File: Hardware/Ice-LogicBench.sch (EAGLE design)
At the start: 114 parts, among them IC1 S27KL0641DABHV020, IC2 S26KL128SDABHI020, IC3 USBLC6-2SC6, IC4 ICE40HX4K-BG121, IC5 FUSB302MPX, IC6 USBLC6-2SC6, J2 QWIIC_RIGHT_ANGLE, Y3 12MZ

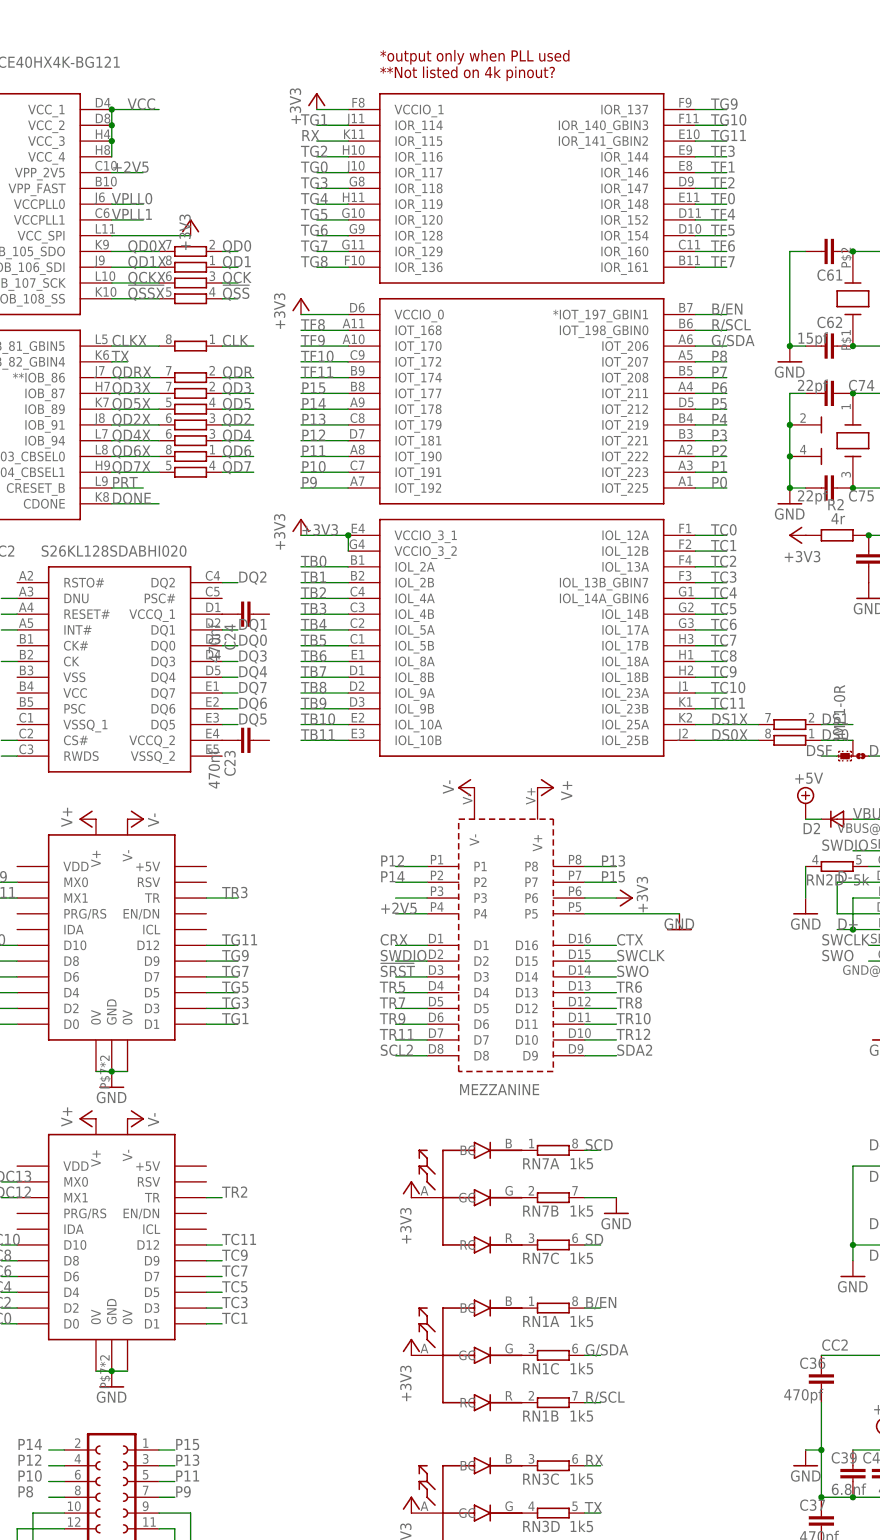
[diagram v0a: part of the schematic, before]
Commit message: REarranged TG/F pinouts for pait matches updated schematic and previews
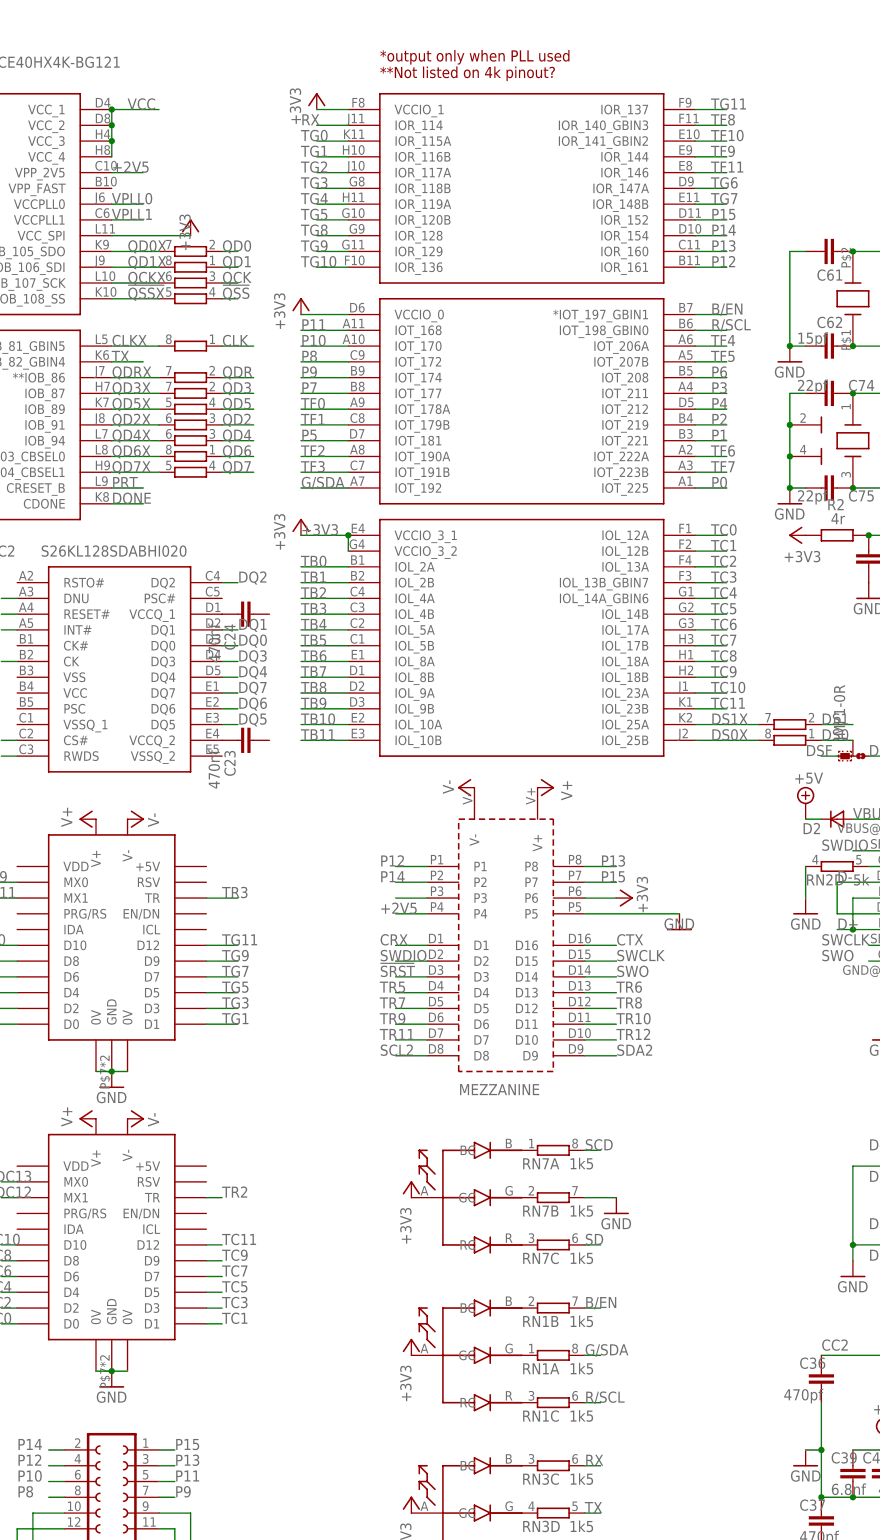
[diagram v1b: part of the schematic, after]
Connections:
- net B/EN: now also RN1B.2; no longer RN1A.2
- net G/SDA: now also IC4.IOT_192, RN1A.2; no longer IC4.IOT_206, RN1C.2
- net N$1: now also RN1A.1; no longer RN1C.1
- net N$3: now also RN1C.1; no longer RN1B.1
- net N$5: now also RN1B.1; no longer RN1A.1
- net P1: now also IC4.IOT_221; no longer IC4.IOT_223
- net P10: now also IC4.IOT_170; no longer IC4.IOT_191
- net P11: now also IC4.IOT_168; no longer IC4.IOT_190
- net P12: now also IC4.IOR_161; no longer IC4.IOT_181
- net P13: now also IC4.IOR_160; no longer IC4.IOT_179
- net P14: now also IC4.IOR_154; no longer IC4.IOT_178
- net P15: now also IC4.IOR_152; no longer IC4.IOT_177
- net P2: now also IC4.IOT_219; no longer IC4.IOT_222
- net P3: now also IC4.IOT_211; no longer IC4.IOT_221
- net P4: now also IC4.IOT_212; no longer IC4.IOT_219
- net P5: now also IC4.IOT_181; no longer IC4.IOT_212
- net P6: now also IC4.IOT_208; no longer IC4.IOT_211
- net P7: now also IC4.IOT_177; no longer IC4.IOT_208
- net P8: now also IC4.IOT_172; no longer IC4.IOT_207
- net P9: now also IC4.IOT_174; no longer IC4.IOT_192
- net R/SCL: now also RN1C.2; no longer RN1B.2
- net RX: now also IC4.IOR_114; no longer IC4.IOR_115
- net TF0: now also IC4.IOT_178A; no longer IC4.IOR_148
- net TF1: now also IC4.IOT_179B; no longer IC4.IOR_146
- net TF10: now also IC4.IOR_141_GBIN2; no longer IC4.IOT_172
- net TF11: now also IC4.IOR_146; no longer IC4.IOT_174
- net TF2: now also IC4.IOT_190A; no longer IC4.IOR_147
- net TF3: now also IC4.IOT_191B; no longer IC4.IOR_144
- net TF4: now also IC4.IOT_206A; no longer IC4.IOR_152
- net TF5: now also IC4.IOT_207B; no longer IC4.IOR_154
- net TF6: now also IC4.IOT_222A; no longer IC4.IOR_160
- net TF7: now also IC4.IOT_223B; no longer IC4.IOR_161
- net TF8: now also IC4.IOR_140_GBIN3; no longer IC4.IOT_168
- net TF9: now also IC4.IOR_144; no longer IC4.IOT_170
- net TG0: now also IC4.IOR_115A; no longer IC4.IOR_117
- net TG1: now also IC4.IOR_116B; no longer IC4.IOR_114
- net TG10: now also IC4.IOR_136; no longer IC4.IOR_140_GBIN3
- net TG11: now also IC4.IOR_137; no longer IC4.IOR_141_GBIN2
- net TG2: now also IC4.IOR_117A; no longer IC4.IOR_116
- net TG3: now also IC4.IOR_118B; no longer IC4.IOR_118
- net TG4: now also IC4.IOR_119A; no longer IC4.IOR_119
- net TG5: now also IC4.IOR_120B; no longer IC4.IOR_120
- net TG6: now also IC4.IOR_147A; no longer IC4.IOR_128
- net TG7: now also IC4.IOR_148B; no longer IC4.IOR_129
- net TG8: now also IC4.IOR_128; no longer IC4.IOR_136
- net TG9: now also IC4.IOR_129; no longer IC4.IOR_137
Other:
- moved on the sheet: RN1A, RN1B, RN1C

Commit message: Temporarily added book by disabling the git ignore until I cal work out the continuous Integration required
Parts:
- removed C30, C43, C74, C75: 22pf, rcl:C-EUC0402
- removed C35, C40, C41, C67, C68, C69, C70, C72: 470nf, rcl:C-EUC0402
- removed C36, C37: 470pf, rcl:C-EUC0402
- removed C38: (no value), rcl:CPOL-EUUD-6,3X8,8
- removed C39: 6.8nf, rcl:C-EUC0402
- removed C42: 22uf, rcl:C-EUC0603
- removed C61, C62: 15pf, rcl:C-EUC0402
- removed C71: 4u7, rcl:C-EUC0402
- removed CAM1, LCD: FH12-24S-0.5SH, con-hirose:FH12-24S-0.5SH
- removed D1: (no value), diode:DIODE-DO214AC
- removed D2: (no value), zetex:DSOD323
- removed D3: (no value), diode:DIODE-SOD323-R
- removed DEBUG: (no value), pinhead:PINHD-2X3/90
- removed H2: HOLE2.5MM-LARGE, amino:HOLE2.5MM-LARGE
- removed J2: QWIIC_RIGHT_ANGLE, SparkFun-Connectors:QWIIC_CONNECTORJS-1MM
- removed JMP1, JMP2: 0R-JUMPC, jump-0r-smd:0R-JUMPC
- removed MEZZANINE: HYPER-TILE, amino:HYPER-TILE
- removed R10: 150k, resistor:R-EU_R0402
- removed RN10, RN11, RN12: 22r, resistor-dil:4R-NEXB38V
- removed SV1, SV2: (no value), con-lsta:FE06-2W
- removed U$11: AT25SDF041A, amino:AT25SDF041A
- removed U$12, U$17: RGB_LED0805, amino:RGB_LED0805
- removed U$20, U$6: (no value), amino:AP3429/A
- removed U$8: USB-C-16, amino:USB-C-16
- removed U$9: NCP114, amino:NCP114
- added B1: PUSH_BUTTON, amino:PUSH_BUTTON
- added BT100: (no value), SparkFun-Batteries:BATTERY-20MM_SMD
- added C100, C102, C103, C104, C106, C107, C108, C109, C110, C111, C112: 470nf, rcl:C-EUC0402
- added C101, C105, C113: 4u7, rcl:C-EUC0402
- added CN1, CN2: USB-C-16, amino:USB-C-16
- added CN3: 2X5-HEADER, amino:2X5-HEADER
- added IC10: FUSB302MPX, SamacSys_Parts:FUSB302MPX
- added IC7, IC8: USBLC6-2SC6, SamacSys_Parts:USBLC6-2SC6
- added J1: QWIIC_RIGHT_ANGLE, SparkFun-Connectors:QWIIC_CONNECTORJS-1MM
- added L1: RGB_LED, amino:RGB_LED
- added L2: (no value), led:LEDCHIPLED_1206
- added R7: 100r, resistor:R-EU_R0402
- added R8: 1k5, resistor:R-EU_R0402
- added RN100, RN101, RN102: 10k, resistor-dil:4R-NEXB38V
- added TILE2: UTILE_LPCARRIER_SMD_MALE_1.27, amino:UTILE_LPCARRIER_SMD_MALE_1.27
- added TILE6: HYPER-TILECARRIER, amino:HYPER-TILECARRIER
- C1, C12, C2, C20, C3, C6: value 470nf -> 22uf; device rcl:C-EUC0402 -> rcl:C-EUC0603
- C11, C27, C5: value 470nf -> 22pf
- C13, C15, C31, C34: value 6.8nf -> 470nf
- C19: value 4u7 -> 22uf; device rcl:C-EUC0402 -> rcl:C-EUC0603
- C21: value 10uf -> 470nf
- C25: value 470nf -> 4u7
- C26: value 22uf -> 15pf; device rcl:C-EUC0603 -> rcl:C-EUC0402
- C28: value 470nf -> 15pf
- C29: value 22uf -> 22pf; device rcl:C-EUC0603 -> rcl:C-EUC0402
- C32, C33: value 6.8nf -> 470pf
- IC1: value S27KL0641DABHV020 -> (none); device SamacSys_Parts:S27KL0641DABHV020 -> amino:AP3429/A
- IC2: value S26KL128SDABHI020 -> NCP114; device SamacSys_Parts:S26KL128SDABHI020 -> amino:NCP114
- IC3: value USBLC6-2SC6 -> ICE40HX4K-BG121; device SamacSys_Parts:USBLC6-2SC6 -> SamacSys_Parts:ICE40HX4K-BG121
- IC4: value ICE40HX4K-BG121 -> AT25SDF041A; device SamacSys_Parts:ICE40HX4K-BG121 -> amino:AT25SDF041A
- IC5: value FUSB302MPX -> (none); device SamacSys_Parts:FUSB302MPX -> amino:AP3429/A
- IC6: value USBLC6-2SC6 -> S27KL0641DABHV020; device SamacSys_Parts:USBLC6-2SC6 -> SamacSys_Parts:S27KL0641DABHV020
- R1: value 27k -> 120k
- R2: value 4r -> 120k
- R3, R4: value 100R -> 100r
- R6: value 100R -> 27k
- R9: value 120k -> 1k
- RN1, RN3: value 1k5 -> 22r
- RN2, RN5: value 5k -> 22r; device resistor-dil:4R-N0603-ARV -> resistor-dil:4R-NEXB38V
- RN4: value 5.1k -> 22r
- RN6, RN9: value 22r -> 5k1
- RN7: value 1k5 -> 5k1
- RN8: value 22r -> 1k5
- U$1: value USB-C-16 -> SS54; device amino:USB-C-16 -> amino:SS54
- U$2: value RGB_LED0805 -> SS54; device amino:RGB_LED0805 -> amino:SS54
- renumbered QD6 to IC9, R14 to R5, U$10 to SD100, U$13 to TILE5, U$23 to I1, U$3 to TILE1, U$30 to TILE3, U$31 to TILE4, U$4 to Y2, U$7 to I2, Y3 to Y1
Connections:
- removed net !CS: IC9.PE15
- removed net !INT: IC5.INT_N
- removed net ADC2/MISO1: IC9.PC2
- removed net ADC3/MOSI1: IC9.PC3
- removed net ADC8/DHS: IC9.PA4
- removed net B/EN: CAM1-17.1, IC4.*IOT_197_GBIN1, RN1B.2
- removed net CC1: C37.1, IC5.CC1_1, IC5.CC1_2, IC6.I/O1_2, U$8.CC1
- removed net CC2: C36.2, IC5.CC2_1, IC5.CC2_2, IC6.I/O2_2, U$8.CC2
- removed net CRX: IC9.PB12, MEZZANINE.D1
- removed net CTX: IC9.PB13, MEZZANINE.D16
- removed net DC2: IC9.PE0
- removed net DC3: IC9.PE1
- removed net DC5: IC9.PD3
- removed net DN: U$8.DN1, U$8.DN2
- removed net DS1: IC1.CS#, RN8B.1
- removed net DS1X: IC4.IOL_25A, RN8B.2
- removed net DSF: IC2.CS#, JMP1-0R.1
- removed net DSR: IC2.DNU, JMP1-0R.3
- removed net DVS: IC9.PB7
- removed net G/SDA: CAM1-22.1, IC4.IOT_192, RN1A.2
- removed net INT: IC2.INT#
- removed net N$15: C23.1, IC2.VCCQ_2
- removed net N$16: C24.1, IC2.VCCQ_1
- removed net N$17: C25.1, IC1.VCCQ_1
- removed net N$20: RN7A.1, U$12.BC
- removed net N$21: RN7B.1, U$12.GC
- removed net N$22: RN7C.1, U$12.RC
- removed net N$23: LCD-1.1, R4.1
- removed net N$24: RN7D.2, U$8.SHLD
- removed net N$25: C41.2, IC9.VDD_2
- removed net N$26: CAM1-23.1, JMP2-0R.2
- removed net N$27: IC3.I/O1_2
- removed net N$28: IC3.I/O2_2
- removed net N$3: RN1C.1, U$17.RC
- removed net N$5: RN1B.1, U$17.BC
- removed net N$7: MEZZANINE.P3
- removed net N$8: RN3A.2, U$1.SHLD
- removed net N$85: C69.2, IC9.VDD_4
- removed net N$86: C67.2, IC9.VDD_3
- removed net N$89: C68.2, IC9.VDD_5
- removed net N$9: RN2D.2, U$1.CC1
- removed net N$90: C71.1, IC9.VBAT
- removed net N$92: C19.1, IC9.VREF+
- removed net QD4: IC9.PD11, RN10C.1
- removed net QD4X: IC4.IOB_94, RN10C.2
- removed net QD5: IC9.PD12, RN10D.1
- removed net QD5X: IC4.IOB_89, RN10D.2
- removed net QD6: IC9.PE2, RN11A.1
- removed net QD6X: IC4.IOB_103_CBSEL0, RN11A.2
- removed net QD7: IC9.PD13, RN11D.1
- removed net QD7X: IC4.IOB_104_CBSEL1, RN11D.2
- removed net QDRX: IC4.**IOB_86, RN10B.2
- removed net R/SCL: CAM1-20.1, IC4.IOT_198_GBIN0, RN1C.2
- removed net TR10: IC9.PD7, MEZZANINE.D11
- removed net TR11: IC9.PB4, MEZZANINE.D7
- removed net TR12: IC9.PB5, MEZZANINE.D10
- removed net TR7: IC9.PD4, MEZZANINE.D5
- removed net TR8: IC9.PD5, MEZZANINE.D12
- removed net TR9: IC9.PD6, MEZZANINE.D6
- removed net V+: C38.+, D1.C, H2.P, H4.P, MEZZANINE.V+, TILE1.V+, TILE3.V+, TILE4.V+, TILE5.V+
- removed net V-: C38.-, H1.P, H3.P, MEZZANINE.V-, TILE1.V-, TILE3.V-, TILE4.V-, TILE5.V-
- removed net VBUS: D2.A, IC3.VBUS, IC6.VBUS, U$1.VBUS
- removed net ~1V8: C31.2, CAM1-15.1, D3.C
- new net !HRST: IC6.RESET#, IC9.PD0
- new net !TRSTA: IC9.PE0, TILE1.PRG/RS, TILE2.PRG/RS, TILE4.PRG/RS
- new net !TRSTB: IC9.PE7, TILE3.PRG/RS, TILE5.PRG/RS
- new net ADC2: IC9.PC2, TILE4.RSV
- new net ADC3: IC9.PC3, TILE1.MX0
- new net B/!WS: IC3.*IOT_197_GBIN1, RN8C.2, TILE6.F23
- new net CC1A: CN1.CC1, RN9B.2, TILE6.E10
- new net CC1B: C33.1, CN2.CC1, IC10.CC1_1, IC10.CC1_2
- new net CC2A: CN1.CC2, RN9A.2, TILE6.E9
- new net CC2B: C32.2, CN2.CC2, IC10.CC2_1, IC10.CC2_2
- new net ENA: IC9.PE1, TILE1.EN/DN, TILE2.EN/DN, TILE4.EN/DN
- new net ENB: IC9.PE8, TILE3.EN/DN, TILE5.EN/DN
- new net G/MT1: IC3.IOT_181, TILE6.F2
- new net GP1: IC9.PD1, TILE6.E23
- new net GP2: IC9.PD3, TILE6.E2
- new net GP3: IC9.PD4, TILE6.E22
- new net GP4: IC9.PD5, TILE6.E3
- new net GP5: IC9.PD6, TILE6.E21
- new net GP6: IC9.PB4, TILE6.E4
- new net GP7: IC9.PB5, TILE6.E19
- new net GP8: IC9.PB7, TILE6.E6
- new net HLD: IC4.HOLD, IC9.PE15
- new net INTU: IC10.INT_N, IC9.PA4
- new net MODE: IC9.PE9, RN8B.2
- new net MT0: IC3.IOR_114, TILE6.F1
- new net R/!DS: IC3.IOT_198_GBIN0, TILE6.F24
- new net RXX: IC3.IOL_25B, RN1A.2
- new net SHA: CN1.SHLD, R8.1
- new net SHB: CN2.SHLD, RN8D.1
- new net TXX: IC3.IOL_25A, RN1B.2
- new net VBAT: BT100.+, C23.1, IC9.VBAT
- new net VBUSA: CN1.VBUS, IC8.VBUS, TILE6.E15, U$2.ANODE
- new net VBUSB: CN2.VBUS, IC10.VBUS, U$1.ANODE
- new net WP: IC4.WP, IC9.PE10
- net !QSS: now also RN4C.1; no longer RN12D.1
- net !QSSX: now also IC3.IOB_104_CBSEL1, RN5D.2; no longer IC4.IOB_108_SS, RN12D.2
- net !SRST: now also C24.2, CN3.6, RN7D.2, TILE6.E17; no longer DEBUG.4, MEZZANINE.D3
- net !SS: now also IC3.IOB_108_SS, IC4.CS, RN102D.1; no longer RN4B.1, U$11.CS
- net +2V5: now also C112.1, C7.2, IC2.VOUT, IC3.VPP_2V5; no longer C27.2, C33.2, C5.1, CAM1-21.1, D3.A, IC4.VPP_2V5, MEZZANINE.P4, U$9.VOUT
- net +3V3: now also B1.P$1, C100.1, C101.2, C102.1, C103.1, C106.1, C108.1, C11.2, C16.2, C17.2, C2.1, C22.2, C3.2, C31.2, C6.2, C8.2, CN3.1, IC10.VDD_1, IC10.VDD_2, IC2.EN, IC2.VIN, IC3.VCCIO_0, IC3.VCCIO_1, IC3.VCCIO_2, IC3.VCCIO_3_1, IC3.VCCIO_3_2, IC3.VCC_SPI, IC4.VCC, IC6.VCCQ_1, IC6.VCCQ_2, IC9.VDD_2, IC9.VDD_3, IC9.VDD_4, IC9.VDD_5, J1.2, L1.ANODE, R7.2, R9.1, RN100A.2, RN100B.2, RN100C.2, RN101A.2, RN101B.2, RN101C.2, RN101D.2, RN102A.2, RN102B.2, RN102C.2, RN102D.2, RN6A.1, RN6B.1, RN7A.1, RN7B.1, RN7C.1, RN7D.1, TILE1.VDD, TILE2.VDD, TILE3.VDD, TILE4.VDD, TILE5.VDD, TILE6.F22; no longer C11.1, C14.2, C18.1, C20.1, C28.2, C29.1, C30.2, C32.2, C34.2, C35.2, C8.1, CAM1-14.1, DEBUG.6, IC4.VCCIO_0, IC4.VCCIO_1, IC4.VCCIO_2, IC4.VCCIO_3_1, IC4.VCCIO_3_2, IC4.VCC_SPI, IC5.VDD_1, IC5.VDD_2, J2.2, JMP2-0R.1, LCD-4.1, LCD-5.1, LCD-6.1, MEZZANINE.P6, R2.2, R4.2, RN1D.2, RN2A.2, RN2B.2, RN4A.2, RN4B.2, RN4C.2, RN4D.2, RN5A.2, RN5B.2, RN5C.2, RN5D.2, SV1.11, SV1.12, SV2.11, SV2.12, U$11.HOLD, U$11.VCC, U$11.WP, U$12.ANODE, U$17.ANODE, U$2.ANODE, U$9.EN, U$9.VIN
- net +5V: now also C1.2, C14.2, C20.1, C34.2, H1.P, IC1.VIN, IC10.VCONN_1, IC10.VCONN_2, IC5.EN, IC5.VIN, IC7.VBUS, TILE1.+5V, TILE2.+5V, TILE3.+5V, TILE4.+5V, TILE5.+5V, TILE6.E11, TILE6.E12, U$2.CATHODE; no longer C26.2, C39.2, C40.2, C42.2, D2.C, IC5.VCONN_1, IC5.VCONN_2, U$20.VIN, U$6.EN, U$6.VIN
- net ADC0: now also TILE4.MX0
- net ADC1: now also TILE4.MX1
- net ADC11: now also TILE3.MX0; no longer TILE5.MX1
- net ADC12: now also TILE3.MX1; no longer TILE4.MX1
- net ADC13: now also TILE3.RSV; no longer TILE4.MX0
- net ADC14: now also TILE2.MX0; no longer TILE1.MX1
- net ADC15: now also TILE2.MX1; no longer TILE1.MX0
- net ADC4: now also TILE1.MX1
- net ADC5: now also TILE1.RSV
- net ADC6: now also TILE5.MX0; no longer TILE3.MX0
- net ADC7: now also TILE5.MX1; no longer TILE3.MX1
- net ADC9: now also TILE5.RSV; no longer TILE5.MX0
- net BOOT: now also B1.P$2, IC9.PD7, RN100D.2, TILE6.E16; no longer RN2C.2
- net CLK: now also RN3D.1; no longer RN10A.1
- net CLKX: now also IC3.*IOB_81_GBIN5, RN3D.2; no longer IC4.*IOB_81_GBIN5, RN10A.2
- net D+: now also CN1.DP1, CN1.DP2, IC8.I/O1_2; no longer IC3.I/O2_1, U$1.DP1, U$1.DP2
- net D-: now also CN1.DN1, CN1.DN2, IC8.I/O2_2; no longer IC3.I/O1_1, U$1.DN1, U$1.DN2
- net DM: now also CN2.DN1, CN2.DN2, IC7.I/O1_1; no longer IC6.I/O1_1
- net DONE: now also IC3.CDONE, IC9.PD14, RN8A.2; no longer IC4.CDONE, IC9.PD15, RN3B.2
- net DP: now also CN2.DP1, CN2.DP2, IC7.I/O2_1; no longer IC6.I/O2_1, U$8.DP1, U$8.DP2
- net DQ0: now also IC6.DQ0, RN2B.1; no longer IC1.DQ0, IC2.DQ0, RN6B.1
- net DQ0X: now also IC3.IOB_63, RN2B.2; no longer IC4.IOB_63, RN6B.2
- net DQ1: now also IC6.DQ1, RN3A.1; no longer IC1.DQ1, IC2.DQ1, RN9B.1
- net DQ1X: now also IC3.IOB_73, RN3A.2; no longer IC4.IOB_73, RN9B.2
- net DQ2: now also IC6.DQ2, RN1C.1; no longer IC1.DQ2, IC2.DQ2, RN8C.1
- net DQ2X: now also IC3.IOB_56, RN1C.2; no longer IC4.IOB_56, RN8C.2
- net DQ3: now also IC6.DQ3, RN4A.1; no longer IC1.DQ3, IC2.DQ3, RN9A.1
- net DQ3X: now also IC3.IOB_79, RN4A.2; no longer IC4.IOB_79, RN9A.2
- net DQ4: now also IC6.DQ4, RN1D.1; no longer IC1.DQ4, IC2.DQ4, RN8D.1
- net DQ4X: now also IC3.IOB_57, RN1D.2; no longer IC4.IOB_57, RN8D.2
- net DQ5: now also IC6.DQ5, RN2C.1; no longer IC1.DQ5, IC2.DQ5, RN6C.1
- net DQ5X: now also IC3.IOB_71, RN2C.2; no longer IC4.IOB_71, RN6C.2
- net DQ6: now also IC6.DQ6, RN3B.1; no longer IC1.DQ6, IC2.DQ6, RN9C.1
- net DQ6X: now also IC3.IOB_72, RN3B.2; no longer IC4.IOB_72, RN9C.2
- net DQ7: now also IC6.DQ7, RN3C.1; no longer IC1.DQ7, IC2.DQ7, RN9D.1
- net DQ7X: now also IC3.IOB_78, RN3C.2; no longer IC4.IOB_78, RN9D.2
- net DQK: now also IC6.CK, RN2A.1; no longer IC1.CK, IC2.CK, RN6A.1
- net DQKX: now also IC3.IOB_61, RN2A.2; no longer IC4.IOB_61, RN6A.2
- net DQR: now also IC6.RWDS, RN2D.1; no longer IC1.RWDS, IC2.RWDS, RN6D.1
- net DQRX: now also IC3.IOB_64, RN2D.2; no longer IC4.IOB_64, RN6D.2
- net DS0: now also IC6.CS#, RN4B.1; no longer JMP1-0R.2, RN8A.1
- net DS0X: now also IC3.IOB_82_GBIN4, RN4B.2; no longer IC4.IOL_25B, RN8A.2
- net GND: now also BT100.-, C100.2, C101.1, C102.2, C103.2, C106.2, C107.1, C108.2, C109.1, C110.1, C112.2, C13.2, C15.2, C16.1, C17.1, C18.1, C19.2, C2.2, C22.1, C23.2, C24.1, C25.2, C29.1, C33.2, C6.1, C8.1, CN1.GND, CN2.GND, CN3.2, CN3.3, CN3.5, H3.P, IC1.GND, IC10.GND_1, IC10.GND_2, IC2.GND, IC3.GND_1, IC3.GND_10, IC3.GND_2, IC3.GND_3, IC3.GND_4, IC3.GND_5, IC3.GND_6, IC3.GND_7, IC3.GND_8, IC3.GND_9, IC4.GND, IC5.GND, IC6.VSS, IC6.VSSQ_1, IC6.VSSQ_2, IC7.GND, IC8.GND, IC9.VSSA, IC9.VSS_2, IC9.VSS_3, IC9.VSS_4, J1.1, L2.C, R6.2, R8.2, RN100D.1, RN8D.2, RN9A.1, RN9B.1, TILE1.V-, TILE2.0V@1, TILE2.0V@2, TILE2.GND, TILE2.V-, TILE3.V-, TILE4.V-, TILE5.V-, TILE6.E13, TILE6.E14, TILE6.F10, TILE6.F11, TILE6.F12, TILE6.F19, TILE6.F7, TILE6.F8, TILE6.F9; no longer C11.2, C18.2, C2.1, C29.2, C33.1, C35.1, C36.1, C37.2, C39.1, C40.1, C42.1, C5.2, C6.2, C61.1, C62.1, C70.2, C72.1, C74.1, C75.1, C8.2, CAM1-10.1, CAM1-24.1, DEBUG.5, IC3.GND, IC4.GND_1, IC4.GND_10, IC4.GND_2, IC4.GND_3, IC4.GND_4, IC4.GND_5, IC4.GND_6, IC4.GND_7, IC4.GND_8, IC4.GND_9, IC5.GND_1, IC5.GND_2, IC6.GND, J2.1, JMP2-0R.3, LCD-2.1, LCD-23.1, LCD-24.1, LCD-3.1, MEZZANINE.P5, R10.2, RN2C.1, RN2D.1, RN3A.1, RN7B.2, RN7D.1, SV1.10, SV1.9, SV2.10, SV2.9, U$1.GND, U$11.GND, U$20.GND, U$6.GND, U$8.GND, U$9.GND
- net GPLL0: now also C104.1, C105.1, IC3.GNDPLL0; no longer C13.1, C16.1, IC4.GNDPLL0
- net GPLL1: now also C111.1, C113.1, IC3.GNDPLL1; no longer C15.1, C17.1, IC4.GNDPLL1
- net N$1: now also L2.A, R9.2; no longer RN1A.1, U$17.GC
- net N$10: now also C29.2; no longer C75.2
- net N$11: now also C27.2; no longer C74.2
- net N$12: now also C26.2; no longer C62.2
- net N$13: now also C28.2; no longer C61.2
- net N$14: now also C15.1, IC9.VCAP2; no longer C22.1, IC1.VCCQ_2
- net N$18: now also C11.1, IC5.FB, R6.1; no longer C30.1, R1.1, U$6.FB
- net N$19: now also IC5.LX; no longer U$6.LX
- net N$2: now also L1.GC, RN8B.1; no longer RN3D.1, U$2.GC
- net N$4: now also L1.RC, RN8A.1; no longer RN3B.1, U$2.RC
- net N$6: now also L1.BC, RN8C.1; no longer RN3C.1, U$2.BC
- net N$87: now also C18.2; no longer C72.2
- net N$88: now also C25.1, IC9.VREF+, R7.1; no longer C70.1, R2.1
- net N$93: now also C5.1, IC1.FB, R1.1, R2.1; no longer C43.1, R10.1, R9.1, U$20.FB
- net N$94: now also IC1.LX; no longer U$20.LX
- net P0: now also IC3.IOT_225, TILE2.RSV; no longer CAM1-3.1, IC4.IOT_225, SV2.8
- net P1: now also IC3.IOT_221, TILE2.TR; no longer CAM1-4.1, IC4.IOT_221, SV2.7
- net P10: now also IC3.IOT_170, TILE2.D4; no longer CAM1-16.1, IC4.IOT_170, SV1.6
- net P11: now also IC3.IOT_168, TILE2.D5; no longer CAM1-18.1, IC4.IOT_168, SV1.5
- net P12: now also IC3.IOR_161, TILE2.D2; no longer IC4.IOR_161, LCD-8.1, MEZZANINE.P1, SV1.4
- net P13: now also IC3.IOR_160, TILE2.D3; no longer IC4.IOR_160, LCD-9.1, MEZZANINE.P8, SV1.3
- net P14: now also IC3.IOR_154, TILE2.D0; no longer IC4.IOR_154, LCD-10.1, MEZZANINE.P2, SV1.2
- net P15: now also IC3.IOR_152, TILE2.D1; no longer IC4.IOR_152, LCD-12.1, MEZZANINE.P7, SV1.1
- net P2: now also IC3.IOT_219, TILE2.IDA; no longer CAM1-5.1, IC4.IOT_219, SV2.6
- net P3: now also IC3.IOT_211, TILE2.ICL; no longer CAM1-6.1, IC4.IOT_211, SV2.5
- net P4: now also IC3.IOT_212, TILE2.D10; no longer CAM1-7.1, IC4.IOT_212, SV2.4
- net P5: now also IC3.IOT_208, TILE2.D12; no longer CAM1-8.1, IC4.IOT_181, SV2.3
- net P6: now also IC3.IOT_192, TILE2.D8; no longer CAM1-9.1, IC4.IOT_208, SV2.2
- net P7: now also IC3.IOT_177, TILE2.D9; no longer CAM1-11.1, IC4.IOT_177, SV2.1
- net P8: now also IC3.IOT_172, TILE2.D6; no longer CAM1-12.1, IC4.IOT_172, SV1.8
- net P9: now also IC3.IOT_174, TILE2.D7; no longer CAM1-13.1, IC4.IOT_174, SV1.7
- net PEN: now also C13.1, IC1.EN, RN7A.2; no longer C6.1, RN1D.1, U$20.EN
- net PRT: now also IC3.CRESET_B, IC9.PD10; no longer CAM1-19.1, IC1.RESET#, IC2.RESET#, IC4.CRESET_B, IC9.PD14, LCD-7.1
- net QCK: now also RN5D.1; no longer RN12C.1
- net QCKX: now also IC3.IOB_103_CBSEL0, RN5A.2; no longer IC4.IOB_107_SCK, RN12C.2
- net QD0: now also IC9.PD11, RN5C.1; no longer IC9.PE7, RN12B.1
- net QD0X: now also IC3.IOB_87, RN5B.2; no longer IC4.IOB_105_SDO, RN12B.2
- net QD1: now also IC9.PD12, RN5B.1; no longer IC9.PE8, RN12A.1
- net QD1X: now also IC3.IOB_89, RN4D.2; no longer IC4.IOB_106_SDI, RN12A.2
- net QD2: now also IC9.PE2, RN4D.1; no longer IC9.PE9, RN11C.1
- net QD2X: now also IC3.IOB_91, RN5C.2; no longer IC4.IOB_91, RN11C.2
- net QD3: now also IC9.PD13, RN5A.1; no longer IC9.PE10, RN11B.1
- net QD3X: now also IC3.IOB_94, RN4C.2; no longer IC4.IOB_87, RN11B.2
- net QDR: now also IC3.**IOB_86, IC9.PD15; no longer IC9.PD10, RN10B.1
- net RX: now also RN1A.1, TILE6.E1; no longer IC4.IOR_114, RN3C.2
- net SCD: now also RN101B.1; no longer RN5B.1, RN7A.2
- net SCK: now also IC3.IOB_107_SCK, IC4.SCK, RN102C.1, TILE6.F3; no longer RN4C.1, U$11.SCK
- net SCL: now also IC10.SCL, RN6A.2, TILE3.ICL, TILE5.ICL, TILE6.F20
- net SCL2: now also J1.4, RN7B.2, TILE1.ICL, TILE4.ICL, TILE6.E20; no longer IC5.SCL, J2.4, MEZZANINE.D8
- net SD: now also RN100A.1; no longer RN7C.2
- net SD0: now also RN100C.1; no longer RN5A.1
- net SD1: now also RN100B.1; no longer RN2B.1
- net SD2: now also RN101D.1; no longer RN5D.1
- net SD3: now also RN101C.1; no longer RN5C.1
- net SDA: now also IC10.SDA, RN6B.2, TILE3.IDA, TILE5.IDA, TILE6.F5
- net SDA2: now also J1.3, RN7C.2, TILE1.IDA, TILE4.IDA, TILE6.E5; no longer IC5.SDA, J2.3, MEZZANINE.D9
- net SDK: now also RN101A.1; no longer RN2A.1
- net SI: now also IC3.IOB_105_SDO, IC4.SI, RN102A.1, TILE6.F21; no longer RN4D.1, U$11.SI
- net SO: now also IC3.IOB_106_SDI, IC4.SO, RN102B.1, TILE6.F4; no longer RN4A.1, U$11.SO
- net SWCLK: now also CN3.9, TILE6.E8; no longer DEBUG.1, MEZZANINE.D15, U$1.SBU2
- net SWDIO: now also CN3.10, TILE6.E7; no longer DEBUG.3, MEZZANINE.D2, U$1.SBU1
- net SWO: now also CN3.8, TILE6.E18; no longer DEBUG.2, MEZZANINE.D14, U$1.CC2
- net TB0: now also IC3.IOL_2A; no longer IC4.IOL_2A
- net TB1: now also IC3.IOL_2B; no longer IC4.IOL_2B
- net TB10: now also IC3.IOL_10A; no longer IC4.IOL_10A
- net TB11: now also IC3.IOL_10B; no longer IC4.IOL_10B
- net TB2: now also IC3.IOL_4A; no longer IC4.IOL_4A
- net TB3: now also IC3.IOL_4B; no longer IC4.IOL_4B
- net TB4: now also IC3.IOL_5A; no longer IC4.IOL_5A
- net TB5: now also IC3.IOL_5B; no longer IC4.IOL_5B
- net TB6: now also IC3.IOL_8A; no longer IC4.IOL_8A
- net TB7: now also IC3.IOL_8B; no longer IC4.IOL_8B
- net TB8: now also IC3.IOL_9A; no longer IC4.IOL_9A
- net TB9: now also IC3.IOL_9B; no longer IC4.IOL_9B
- net TC0: now also IC3.IOL_12A; no longer IC4.IOL_12A
- net TC1: now also IC3.IOL_12B; no longer IC4.IOL_12B
- net TC10: now also IC3.IOL_23A; no longer IC4.IOL_23A
- net TC11: now also IC3.IOL_23B; no longer IC4.IOL_23B
- net TC2: now also IC3.IOL_13A; no longer IC4.IOL_13A
- net TC3: now also IC3.IOL_13B_GBIN7; no longer IC4.IOL_13B_GBIN7
- net TC4: now also IC3.IOL_14A_GBIN6; no longer IC4.IOL_14A_GBIN6
- net TC5: now also IC3.IOL_14B; no longer IC4.IOL_14B
- net TC6: now also IC3.IOL_17A; no longer IC4.IOL_17A
- net TC7: now also IC3.IOL_17B; no longer IC4.IOL_17B
- net TC8: now also IC3.IOL_18A; no longer IC4.IOL_18A
- net TC9: now also IC3.IOL_18B; no longer IC4.IOL_18B
- net TF0: now also IC3.IOT_178A; no longer IC4.IOT_178A
- net TF1: now also IC3.IOT_179B; no longer IC4.IOT_179B
- net TF10: now also IC3.IOR_141_GBIN2; no longer IC4.IOR_141_GBIN2
- net TF11: now also IC3.IOR_146; no longer IC4.IOR_146
- net TF2: now also IC3.IOT_190A; no longer IC4.IOT_190A
- net TF3: now also IC3.IOT_191B; no longer IC4.IOT_191B
- net TF4: now also IC3.IOT_206A; no longer IC4.IOT_206A
- net TF5: now also IC3.IOT_207B; no longer IC4.IOT_207B
- net TF6: now also IC3.IOT_222A; no longer IC4.IOT_222A
- net TF7: now also IC3.IOT_223B; no longer IC4.IOT_223B
- net TF8: now also IC3.IOR_140_GBIN3; no longer IC4.IOR_140_GBIN3
- net TF9: now also IC3.IOR_144; no longer IC4.IOR_144
- net TG0: now also IC3.IOR_115A; no longer IC4.IOR_115A
- net TG1: now also IC3.IOR_116B; no longer IC4.IOR_116B
- net TG10: now also IC3.IOR_136; no longer IC4.IOR_136
- net TG11: now also IC3.IOR_137; no longer IC4.IOR_137
- net TG2: now also IC3.IOR_117A; no longer IC4.IOR_117A
- net TG3: now also IC3.IOR_118B; no longer IC4.IOR_118B
- net TG4: now also IC3.IOR_119A; no longer IC4.IOR_119A
- net TG5: now also IC3.IOR_120B; no longer IC4.IOR_120B
- net TG6: now also IC3.IOR_147A; no longer IC4.IOR_147A
- net TG7: now also IC3.IOR_148B; no longer IC4.IOR_148B
- net TG8: now also IC3.IOR_128; no longer IC4.IOR_128
- net TG9: now also IC3.IOR_129; no longer IC4.IOR_129
- net TR1: now also IC9.PB13, TILE3.TR; no longer IC9.PD8, TILE1.TR
- net TR2: now also IC9.PB12, TILE5.TR; no longer IC9.PD9, TILE4.TR
- net TR3: now also TILE4.TR; no longer TILE5.TR
- net TR4: now also TILE1.TR; no longer TILE3.TR
- net TR5: now also IC9.PD8; no longer IC9.PD0, MEZZANINE.D4
- net TR6: now also IC9.PD9; no longer IC9.PD1, MEZZANINE.D13
- net TX: now also RN1B.1, TILE6.E24; no longer IC4.IOB_82_GBIN4, RN3D.2
- net VB+: now also C19.1, H4.P, TILE1.V+, TILE2.V+, TILE3.V+, TILE4.V+, TILE5.V+, TILE6.F13, TILE6.F14, TILE6.F15, TILE6.F16, TILE6.F17, TILE6.F18, U$1.CATHODE; no longer D1.A, IC5.VBUS, U$8.VBUS
- net VCC: now also C107.2, C109.2, C110.2, C5.2, IC3.VCC_1, IC3.VCC_2, IC3.VCC_3, IC3.VCC_4, R2.2, R3.1, R4.2; no longer C1.2, C2.2, C3.2, C43.2, C7.2, IC4.VCC_1, IC4.VCC_2, IC4.VCC_3, IC4.VCC_4, R3.2, R6.1, R9.2
- net VPLL0: now also C104.2, C105.2, IC3.VCCPLL0, R4.1; no longer C13.2, C16.2, IC4.VCCPLL0, R3.1
- net VPLL1: now also C111.2, C113.2, IC3.VCCPLL1, R3.2; no longer C15.2, C17.2, IC4.VCCPLL1, R6.2
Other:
- note added: "Add 5v in pad"
- note added: "Add Fuse or foldback protection"
- note added: "Add location holes to tile sockets"
- note added: "Add paste layer for usb shield legs"
- note added: "C/D"
- note added: "Replace 1k5 shield resistor with 5k1 fromRN9"
- note added: "Replace RN7D with RN9 (srst)"
- note added: "Replace boot button with R/A version like mez"
- note added: "STM Uart connection?"
- note added: "TODO Flip horizontally debugs should be 1-5"
- note added: "lc"
- note added: "ld"
- note added: "nLs"
- note added: "what V?"
- note removed: "2xint?"
- moved on the sheet: C1, C10, C11, C12, C13, C14, C15, C16, C17, C18, C19, C2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
